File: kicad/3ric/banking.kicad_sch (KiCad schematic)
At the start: 11 parts

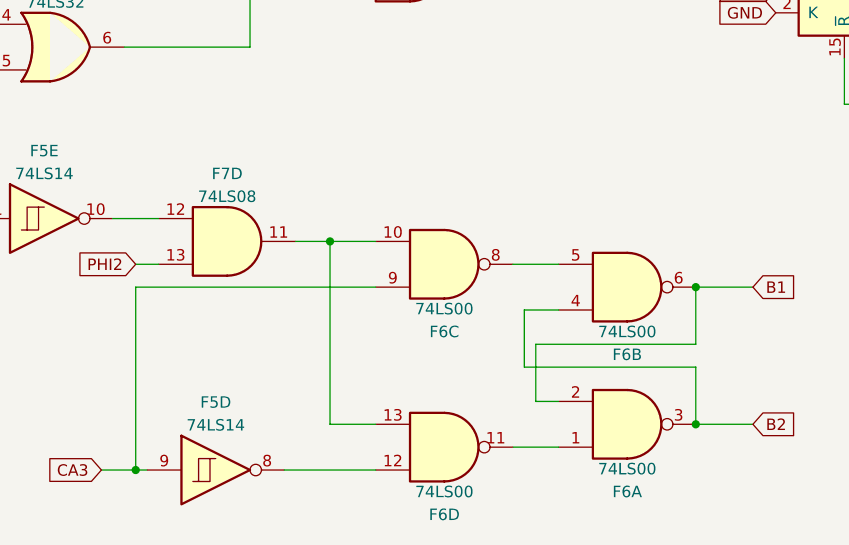
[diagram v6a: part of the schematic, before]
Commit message: update schematic with corrections found via virutal wiring
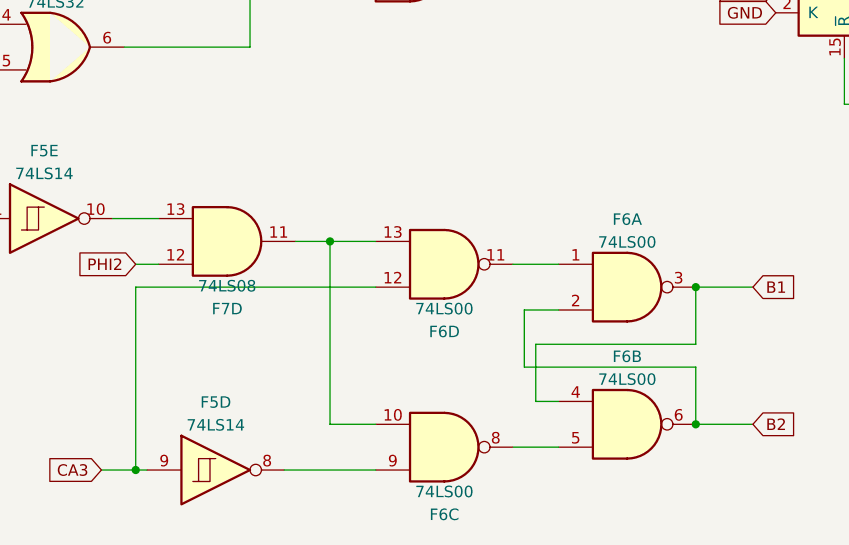
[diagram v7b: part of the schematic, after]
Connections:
- net B1: now also F6.3, F6.4; no longer F6.2, F6.6
- net B2: now also F6.2, F6.6; no longer F6.3, F6.4
- net CA3: now also F6.12; no longer F6.9
- net PHI2: now also F7.12; no longer F7.13
- net at F5.10: now also F7.13; no longer F7.12
- net at F5.8: now also F6.9; no longer F6.12

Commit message: cleaning up of the schematic
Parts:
- removed G1: 74LS112, symbol 74xx:74LS112
- removed Y_SPEAKER: Speaker, symbol Device:Speaker
- added CON2: SJ-3523-SMT-TR, digikey-footprints:Switch_Slide_11.6x4mm_SJ-3523-SMT, symbol dk_Barrel-Audio-Connectors:SJ-3523-SMT-TR
- added unit 2 of F2
- added unit 1 of F2
- added unit 4 of F2
- added unit 2 of F4
- added unit 3 of F5
- added unit 2 of F5
- added unit 2 of F7
- added unit 3 of F7
- added unit 1 of F7
- E1, E2, F1, F2, F5, F6, F7: footprint (none) -> Package_DIP:DIP-14_W7.62mm_Socket
- F3, F4: footprint (none) -> Package_DIP:DIP-16_W7.62mm_Socket
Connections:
- net C030: now also F4.13 (C)
- net GND: now also CON2.1 (S)
- net VCC: now also F4.10 (~{S}), F4.11 (J), F4.12 (K), F4.14 (~{R})
- new net: CON2.2 (T), CON2.3 (R), F4.9 (Q)
- no-connect marks 0 -> 24
